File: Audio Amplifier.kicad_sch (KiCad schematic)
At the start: 0 parts

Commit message: initial commit
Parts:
- added 4ohm20W (x2): Speaker, symbol Device:Speaker
- added U1: TPA3221DDV, DDV0044D_N, symbol Audio Amplifier:TPA3221DDV

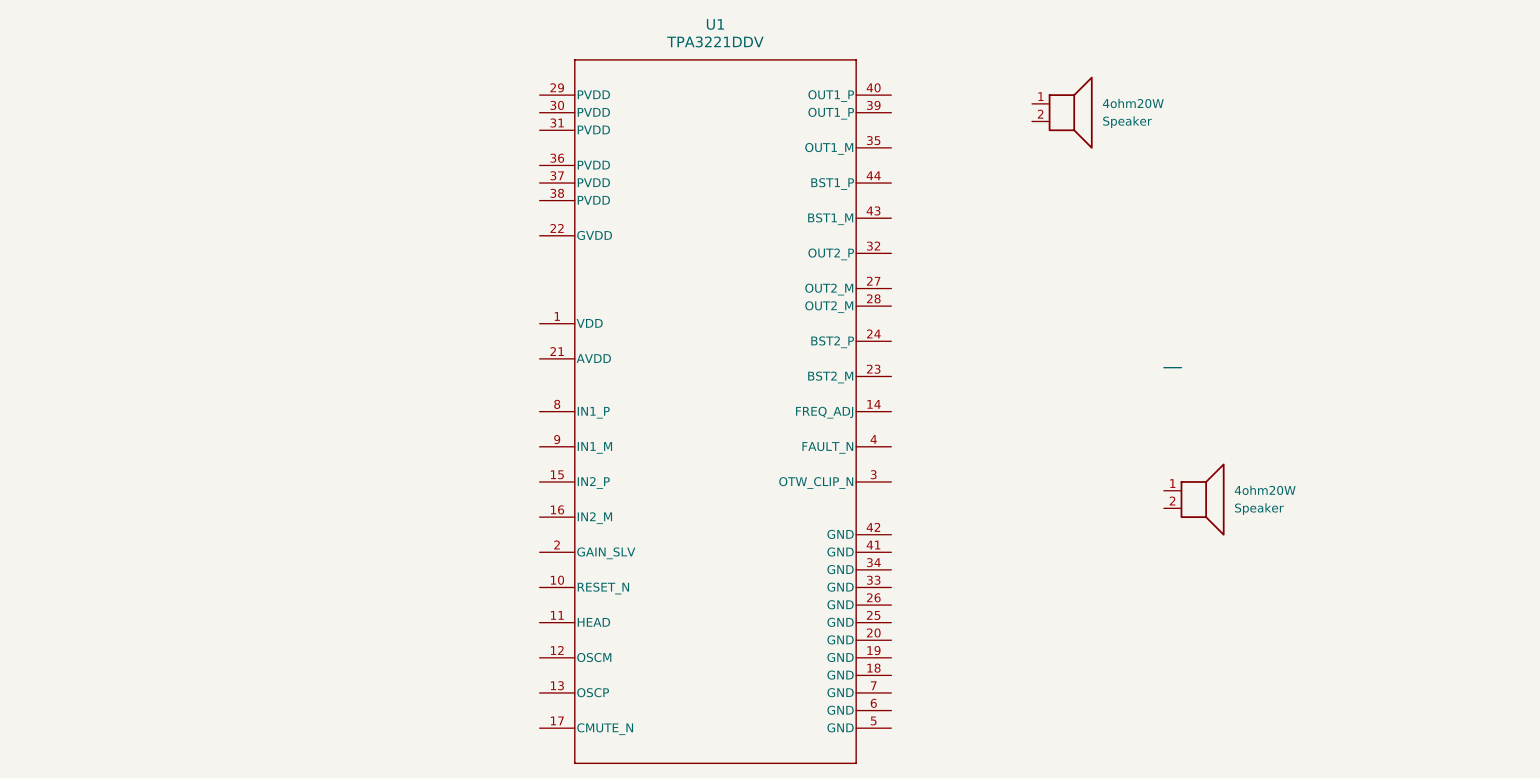
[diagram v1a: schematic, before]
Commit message: Switch to TPA3110d2, Speakers wired in series with basic LC filter used.
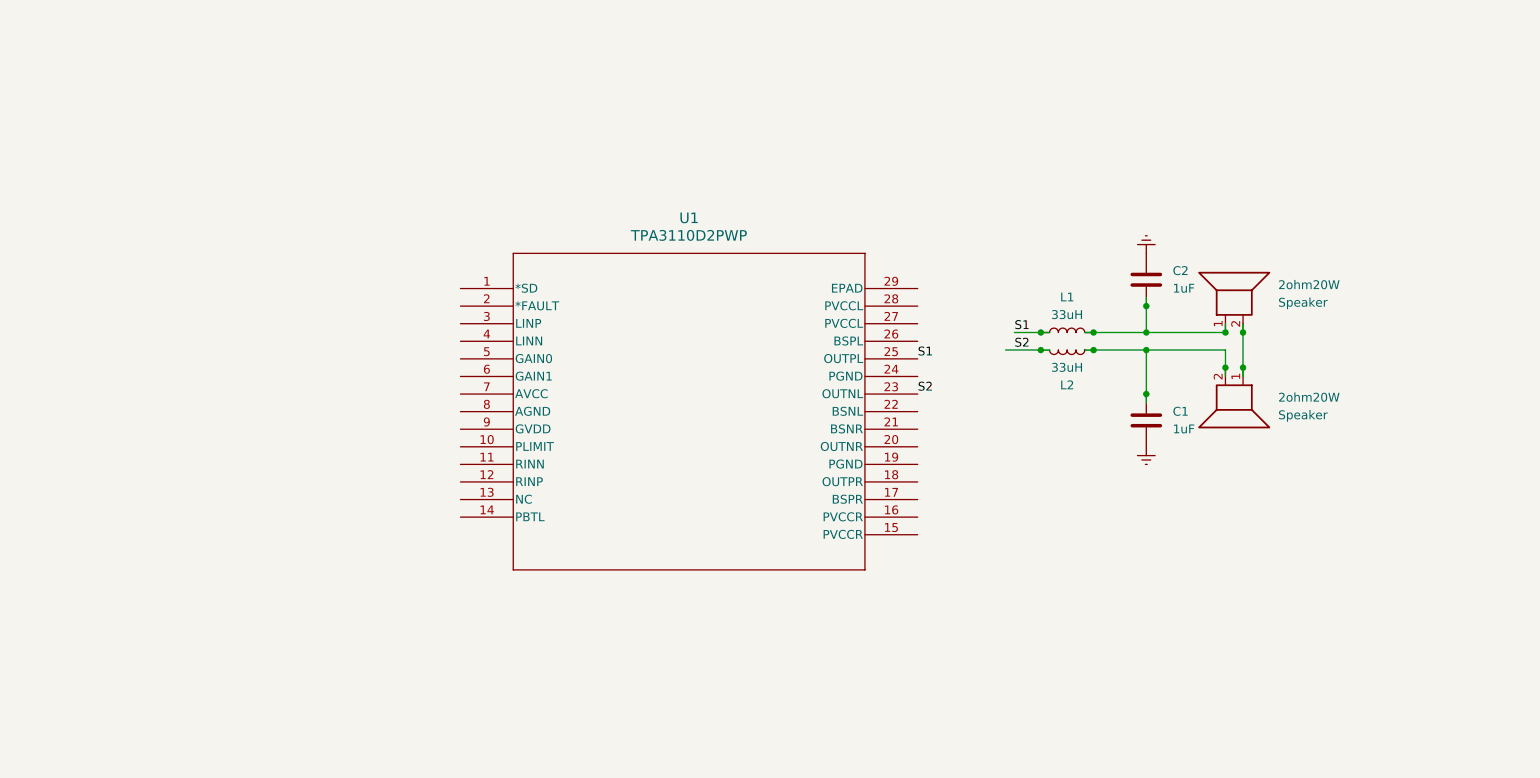
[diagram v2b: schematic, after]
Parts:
- removed U1: TPA3221DDV, DDV0044D_N, symbol Audio Amplifier:TPA3221DDV
- added C1, C2: 1uF, symbol Device:C
- added L1, L2: 33uH, symbol Device:L
- added U1: TPA3110D2PWP, PWP28_6P17X2P4, symbol Audio Amplifier:TPA3110D2PWP
- renumbered 4ohm20W to 2ohm20W
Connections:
- net at 2ohm20W.1: now also 2ohm20W.2
- net at 2ohm20W.2: now also C1.1, L2.1
- net at 2ohm20W.1: now also C2.2, L1.2
- new net Earth: C2.1
- new net S1: L1.1, U1.25 (OUTPL)
- new net S2: L2.2, U1.23 (OUTNL)
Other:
- moved on the sheet: 2ohm20W

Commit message: Feat(PVCC): Adding PVCC to the PVCCR and PVCCL pins on the TPA3110d2
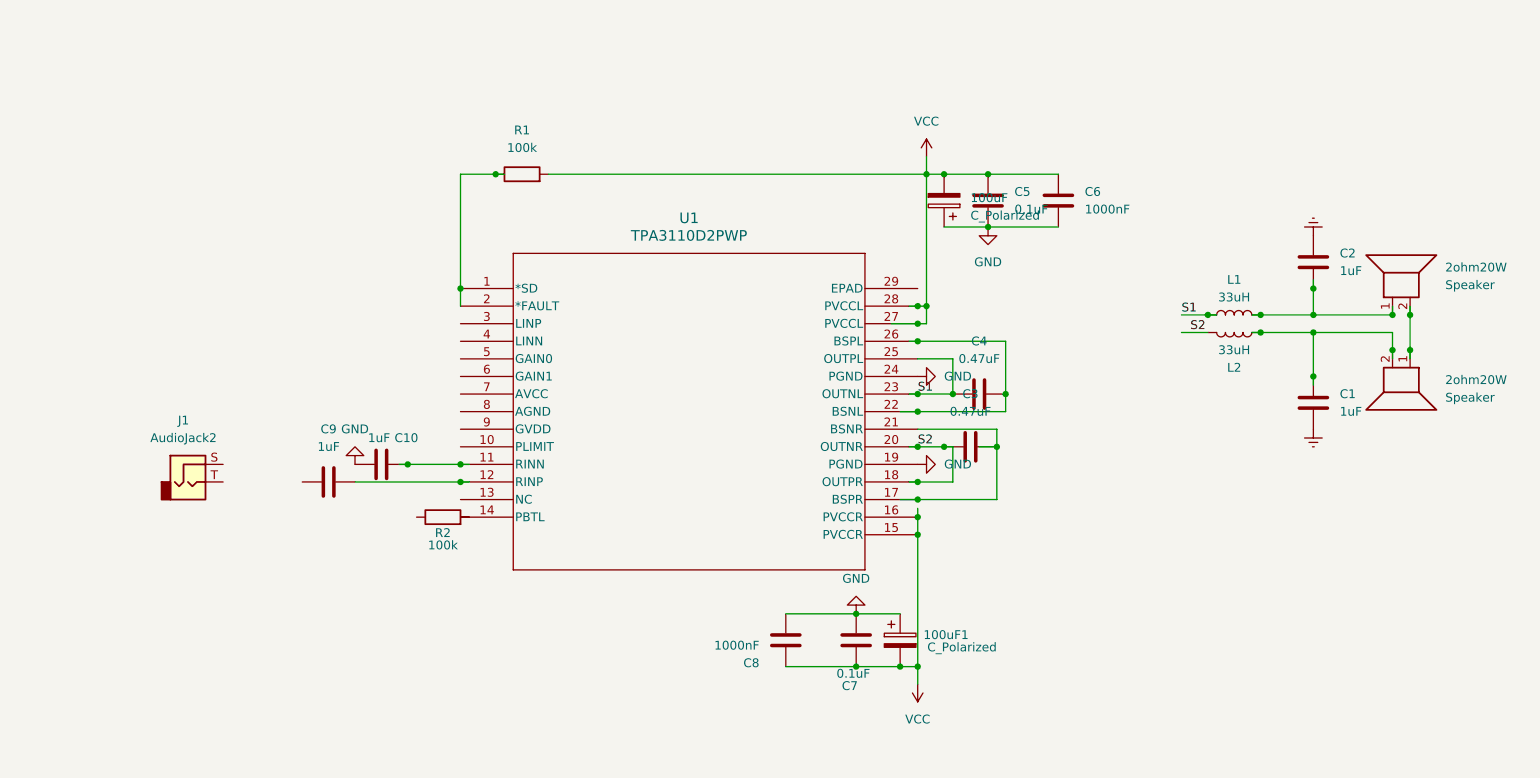
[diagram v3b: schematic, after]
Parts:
- added 100uF, 100uF1: C_Polarized, symbol Device:C_Polarized
- added C10, C9: 1uF, symbol Device:C
- added C3, C4: 0.47uF, symbol Device:C
- added C5, C7: 0.1uF, symbol Device:C
- added C6, C8: 1000nF, symbol Device:C
- added J1: AudioJack2, symbol Connector_Audio:AudioJack2
- added R1, R2: 100k, symbol Device:R
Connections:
- net S1: now also U1.23 (OUTNL), C4.1
- net S2: now also U1.18 (OUTPR), U1.20 (OUTNR), C3.1; no longer U1.23 (OUTNL)
- net at U1.1 (*SD): now also U1.2 (*FAULT), R1.1
- net at U1.11 (RINN): now also C10.2
- net at U1.12 (RINP): now also C9.2
- net VCC: now reaches U1.15 (PVCCR)
- net VCC: now also U1.16 (PVCCR), U1.27 (PVCCL), U1.28 (PVCCL), 100uF.2, 100uF1.2, C5.1, C6.1, C7.1, C8.1, R1.2
- net at U1.17 (BSPR): now also U1.21 (BSNR), C3.2
- net GND: now reaches U1.19 (PGND)
- net GND: now also U1.24 (PGND), 100uF.1, 100uF1.1, C10.1, C5.2, C6.2, C7.2, C8.2
- net at U1.22 (BSNL): now also U1.26 (BSPL), C4.2
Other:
- moved on the sheet: 2ohm20W, C1, C2, L1, L2

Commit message: Feat(Input): Using a stereo AudioJack3 footprint in KiCAD, tied the ring and tip together for mono input into TPA3110d2. Connected Sleeve to AGND
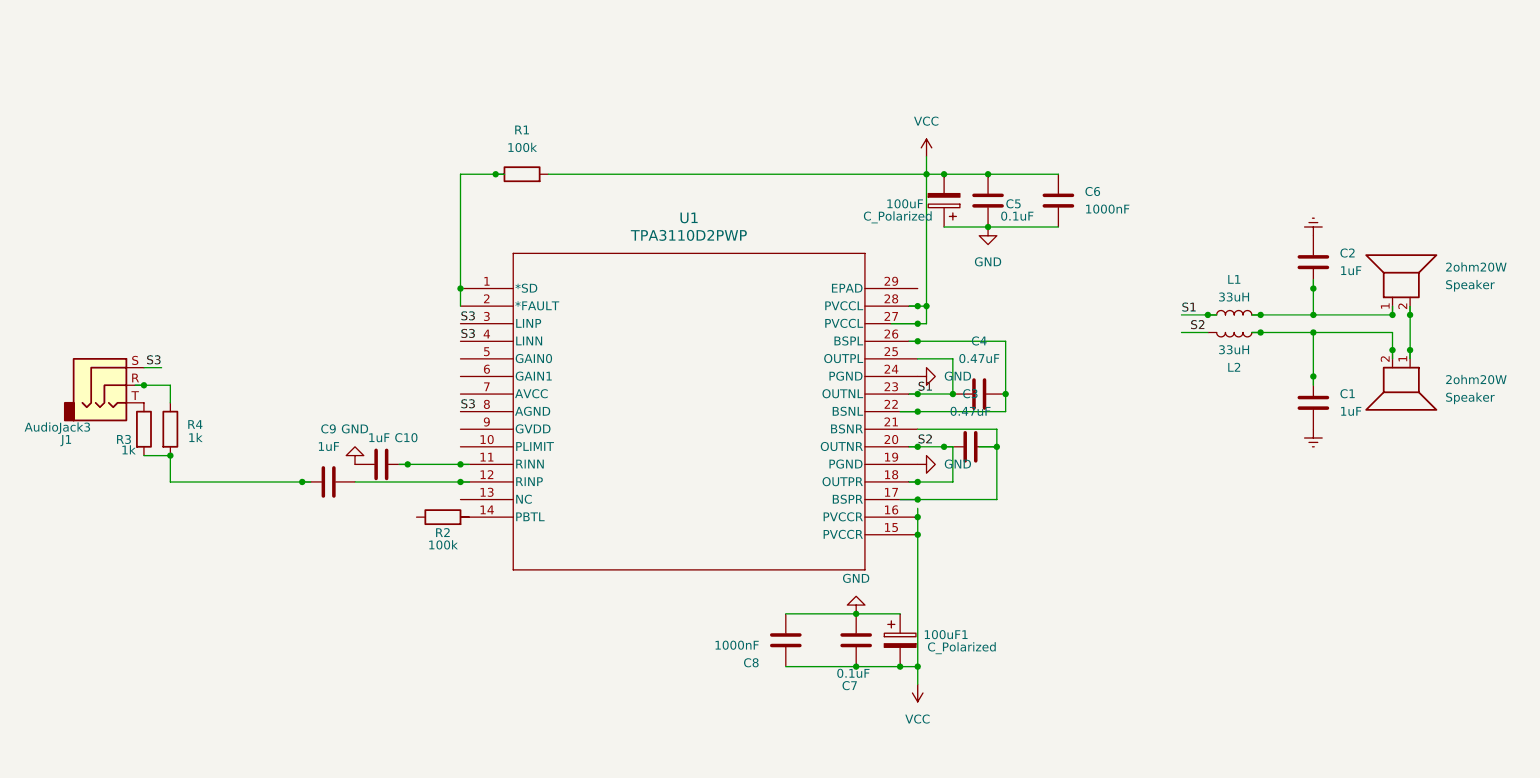
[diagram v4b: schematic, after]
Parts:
- removed J1: AudioJack2, symbol Connector_Audio:AudioJack2
- added J1: AudioJack3, symbol Connector_Audio:AudioJack3
- added R3, R4: 1k, symbol Device:R
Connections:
- net S3: now reaches U1.3 (LINP)
- net S3: now also U1.4 (LINN), U1.8 (AGND), J1.S
- net at C9.1: now also R3.2, R4.2
- new net: J1.R, R4.1
- new net: J1.T, R3.1

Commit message: Feat(AVCC): Wired the AVCC from the PVCC main, finishing the circuit for the PBTL mode. Includes a small toggle switch for standby mode on the SD pin.
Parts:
- added C11, C12: C, symbol Device:C
- added R5: 10, symbol Device:R
- added R6: 1k, symbol Device:R
- added SW1: SW_SPST, symbol Switch:SW_SPST
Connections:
- net GND: now also SW1.1 (A)
- net VCC: now also R5.1
- net at R1.1, U1.1 (*SD), U1.2 (*FAULT): now also R6.1
- net GDVV: now reaches U1.10 (PLIMIT)
- net AVCC: now reaches U1.7 (AVCC)
- net AVCC: now also R2.1, C11.2, C12.1
- net GVDD: now reaches U1.9 (GVDD)
- net GVDD: now also C12.2
- new net: R6.2, SW1.2 (B)
- new net: C11.1, R5.2

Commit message: Fix(Input): Added a potentiometer for volume control, fixed the GDVV from GVDD, fixed the AVCC circuit.
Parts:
- added RV1: 10k Logarithmic, symbol Device:R_Potentiometer
- C11, C12: value C -> 1uF
- renumbered 100uF to 100uF2, 2ohm20W to 2ohm20W1, 2ohm20W to 2ohm20W2
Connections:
- net GDVV is gone; now on net GVDD: U1.10 (PLIMIT)
- net S3 is gone; now on net GND: J1.S, U1.3 (LINP), U1.4 (LINN), U1.8 (AGND)
- net AVCC: now also C11.1, R5.2; no longer C11.2, C12.1
- net GND: now also 100uF1.2, 100uF2.2, C11.2, C12.1, RV1.3; no longer 100uF1.1, 100uF2.1
- net VCC: now also 100uF1.1, 100uF2.1; no longer 100uF1.2, 100uF2.2
- net at R3.2, R4.2: now also RV1.1; no longer C9.1
- new net: C9.1, RV1.2
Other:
- moved on the sheet: 100uF1, 100uF2, R2

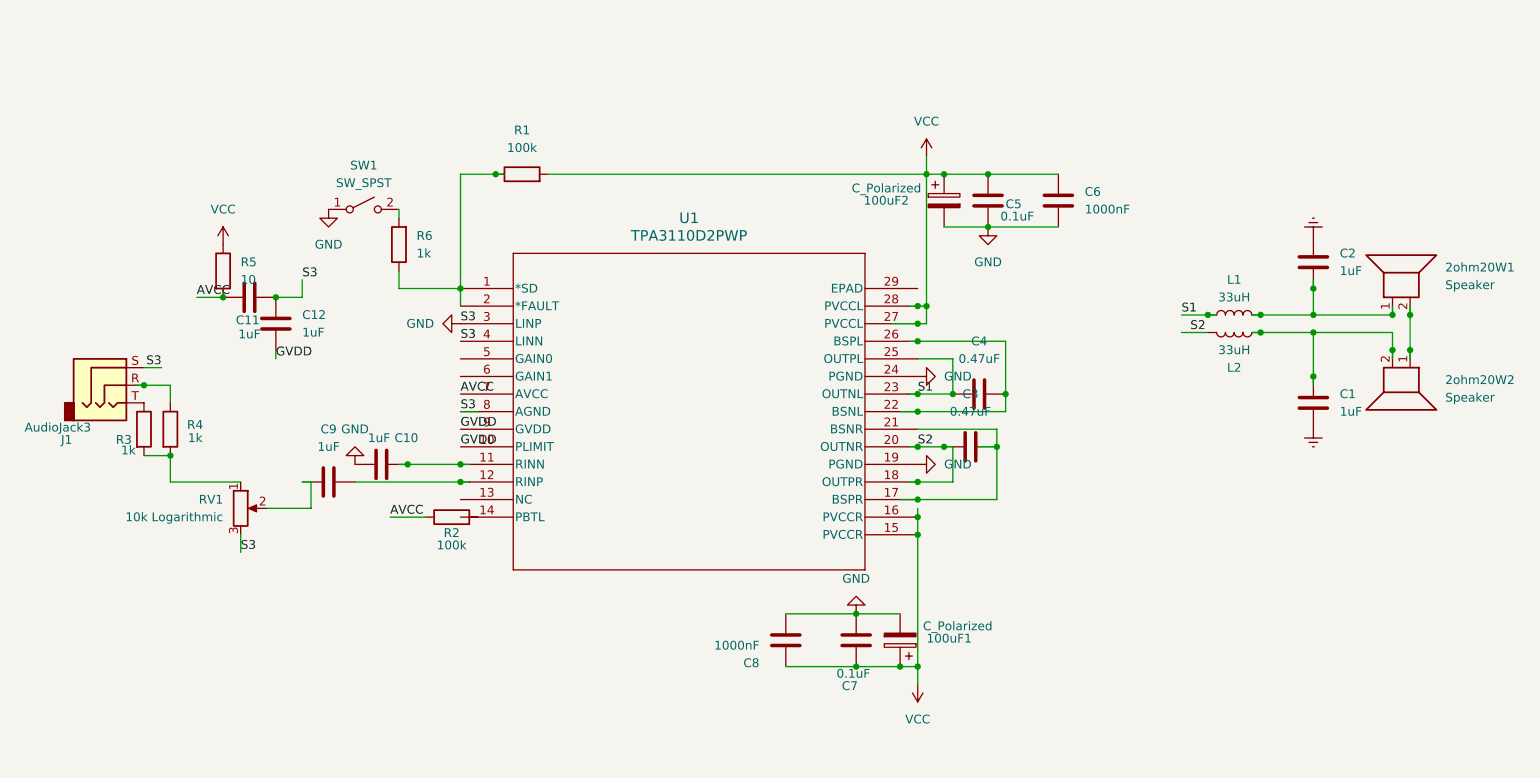
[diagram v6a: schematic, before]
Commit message: Feat(Output): Switched to a stereo audio system, as well as changing the speakers to a 4ohm15W setup.
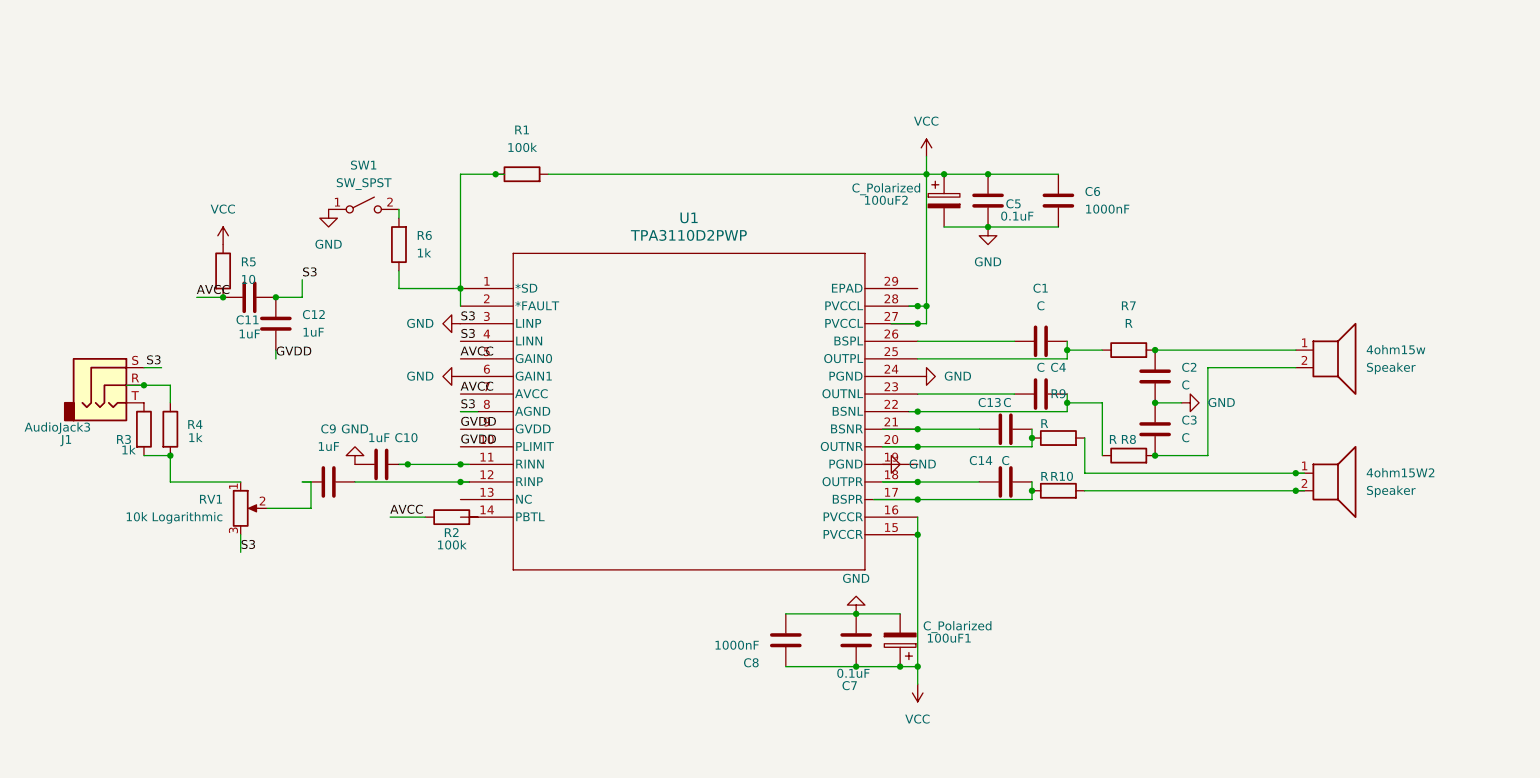
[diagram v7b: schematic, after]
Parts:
- removed L1, L2: 33uH, symbol Device:L
- added C13, C14: C, symbol Device:C
- added R10, R7, R8, R9: R, symbol Device:R
- C1, C2: value 1uF -> C
- C3, C4: value 0.47uF -> C
- renumbered 2ohm20W2 to 4ohm15W2, 2ohm20W1 to 4ohm15w
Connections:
- net Earth is gone; now on an unnamed net: C2.1
- net AVCC: now also U1.5 (GAIN0)
- net GND: now also C2.2, C3.1, U1.6 (GAIN1); no longer U1.19 (PGND)
- net at C4.2, U1.22 (BSNL): now also R8.1; no longer U1.26 (BSPL)
- net at 4ohm15w.1: now also R7.2; no longer C2.2
- net at C1.1: now also U1.26 (BSPL); no longer 4ohm15W2.2
- net at 4ohm15w.2: now also C3.2, R8.2; no longer 4ohm15W2.1
- net at C1.2: now also U1.25 (OUTPL), R7.1
- net S1: no longer names the net of C4.1, U1.23 (OUTNL)
- net S1: no longer U1.25 (OUTPL)
- removed net S2: C3.1, U1.18 (OUTPR), U1.20 (OUTNR)
- new net: C14.2, R10.1, U1.17 (BSPR)
- new net: C14.1, U1.18 (OUTPR)
- new net: C13.2, R9.1, U1.20 (OUTNR)
- new net: C13.1, U1.21 (BSNR)
- new net: 4ohm15W2.2, R10.2
- new net: 4ohm15W2.1, R9.2
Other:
- moved on the sheet: 4ohm15W2, 4ohm15w
